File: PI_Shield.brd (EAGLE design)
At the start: 160 x 100 mm, 29 parts, among them Q2 220mA/50V/3.5Ω, Y1 ECS-80-S-4X

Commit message: Minor Changes with Schematic
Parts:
- moved PCB1 157.5 mm to (57.1, 1.27), turned to 90 degrees
- moved U$1 73.8 mm to (14.3, 18.0)
- moved U$3 51.7 mm to (23.4, 53.2)
- moved Y1 34.1 mm to (-66.3, 33.3)
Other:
- board size 160 x 100 mm -> 60 x 66.5 mm

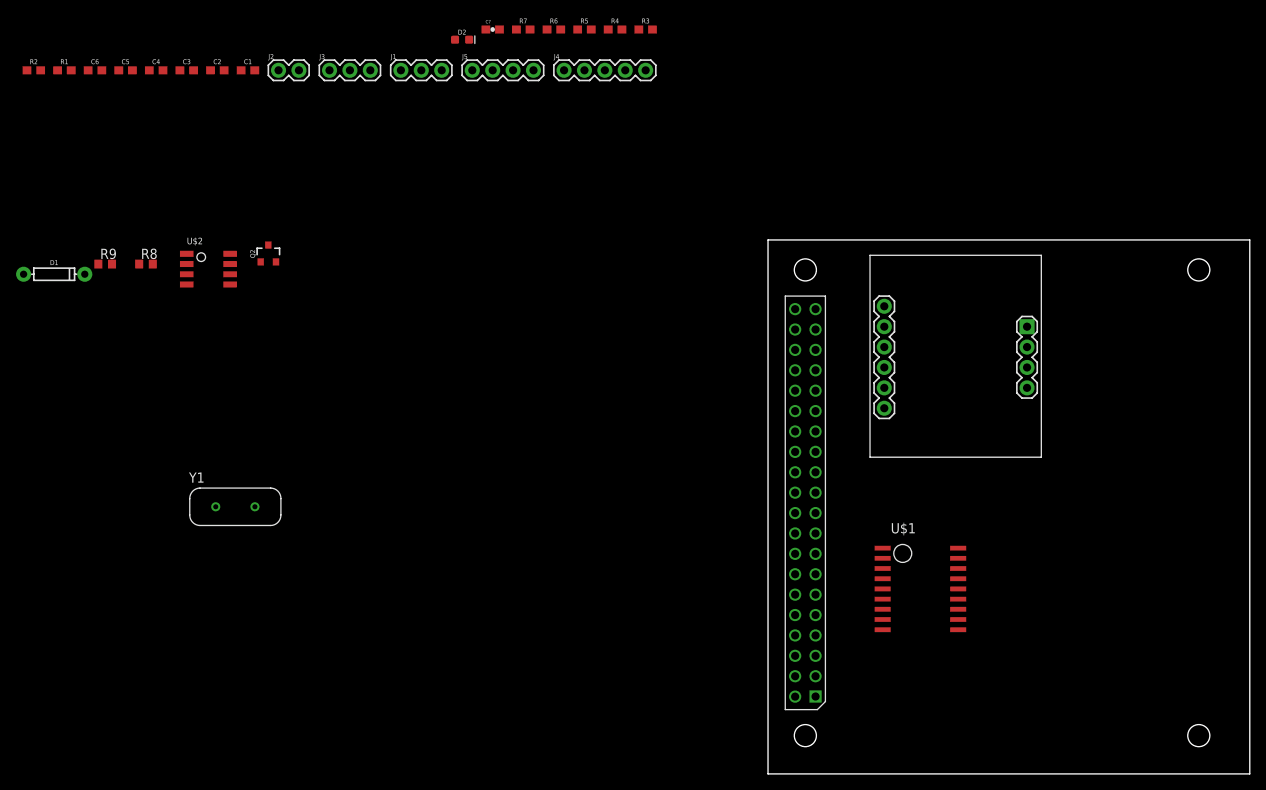
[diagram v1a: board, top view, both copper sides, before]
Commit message: Starting to Route Board
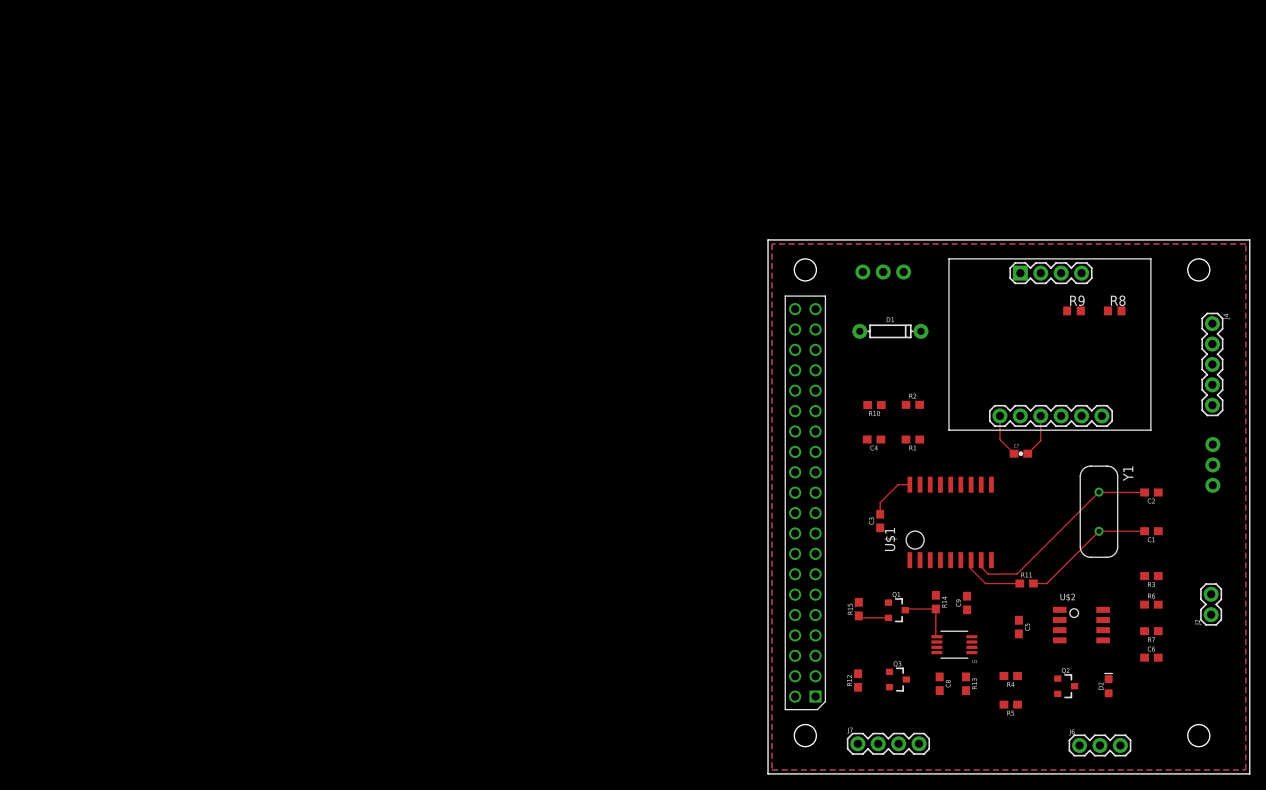
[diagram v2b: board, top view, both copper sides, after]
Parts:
- removed J5: (no value), SparkFun-Connectors:1X04
- added C8, C9: .1uF, SparkFun-Capacitors:0603
- added J6: (no value), SparkFun-Connectors:1X03
- added J7: (no value), SparkFun-Connectors:1X04
- added Q1, Q3: 220mA/50V/3.5Ω, SparkFun-DiscreteSemi:SOT23-3
- added R10: 47, SparkFun-Resistors:0603
- added R11: 0, SparkFun-Resistors:0603
- added R12, R13, R14, R15: 10k, SparkFun-Resistors:0603
- added U1: MAX1136EUA-T, MAX1136EUA-T:21-0036K
- C1, C2: value 22pF -> 18pF
- R3: value (none) -> 0
- moved C6 150.5 mm to (47.8, 14.5)
- moved J2 134.5 mm to (55.2, 19.8), turned to 90 degrees
- moved C5 131.1 mm to (31.2, 18.3), turned to 270 degrees
- moved C2 127.7 mm to (47.8, 35.1), turned to 180 degrees
- moved C1 126.3 mm to (47.8, 30.2), turned to 180 degrees
- moved J3 121.5 mm to (55.4, 35.9), flipped to the bottom, turned to 90 degrees
- moved R8 120.8 mm to (43.2, 57.7)
- moved R9 120.8 mm to (38.1, 57.7)
- moved U$2 117.4 mm to (36.3, 16.6)
- moved R2 117.1 mm to (18.0, 46.0)
- moved R1 115.2 mm to (18.0, 41.7), turned to 180 degrees
- moved D2 113.9 mm to (42.4, 10.9), turned to 90 degrees
- moved Q2 113.0 mm to (37.1, 10.9), turned to 270 degrees
- moved R7 108.3 mm to (47.8, 17.8), turned to 180 degrees
- moved Y1 107.6 mm to (41.2, 32.7), turned to 270 degrees
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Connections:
- new net AIN: J6.1, U1.1
- new net N$6: D1.A, R10.2
- new net N$7: C8.2
- new net SCL_ADC: Q1.3, R14.2, U1.5
- new net SDA_ADC: Q3.3, R13.2, U1.6
- net 3V3: now also Q1.1, Q3.1, R12.2, R15.2
- net 5V: now also C8.1, C9.1, J6.2, J7.4, R13.1, R14.1, U1.4, U1.8; no longer J5.4
- net GND: now also C9.2, J6.3, J7.1, U1.7; no longer J5.1
- net IMU_RESET: now also PCB1.P$33; no longer PCB1.P$7
- net INT: now also PCB1.P$35, U$3.INT; no longer PCB1.P$26
- net N$3: now also R10.1; no longer D1.A
- net OSC2: now also R11.1, R11.2
- net RESET: now also PCB1.P$15; no longer PCB1.P$22
- net SCL: now also J7.2, Q1.2, R15.1; no longer J5.2
- net SDA: now also J7.3, Q3.2, R12.1; no longer J5.3
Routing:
- net OSC1: track 0.00 -> 25.8 mm
- net OSC2: track 0.00 -> 24.5 mm
- net 3V3: track 0.00 -> 11.5 mm
- net SCL_ADC: track 0.00 -> 7.36 mm
- net GND: track 0.00 -> 5.38 mm
- net SCL: track 0.00 -> 3.79 mm
- added copper zone on layer 1, net GND
- added copper zone on layer 16, net GND

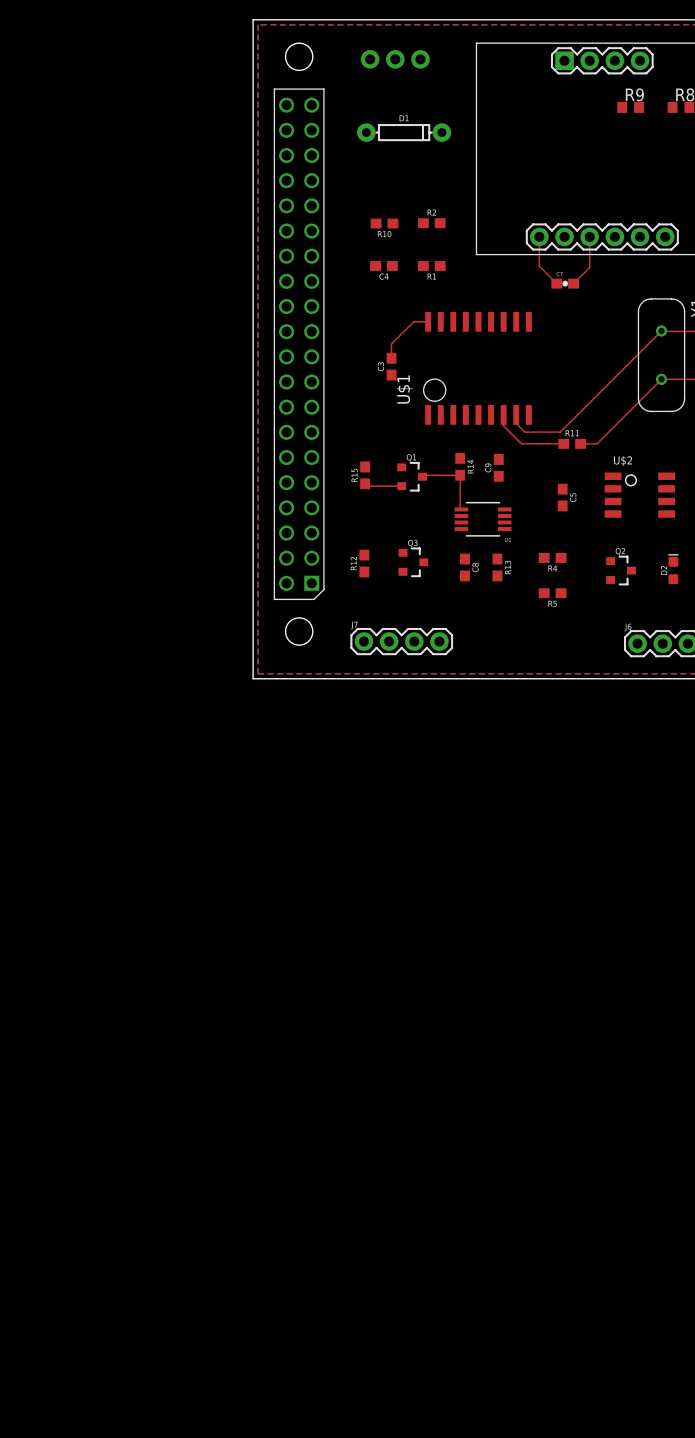
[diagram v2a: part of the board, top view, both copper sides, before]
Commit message: Added Current Sensor
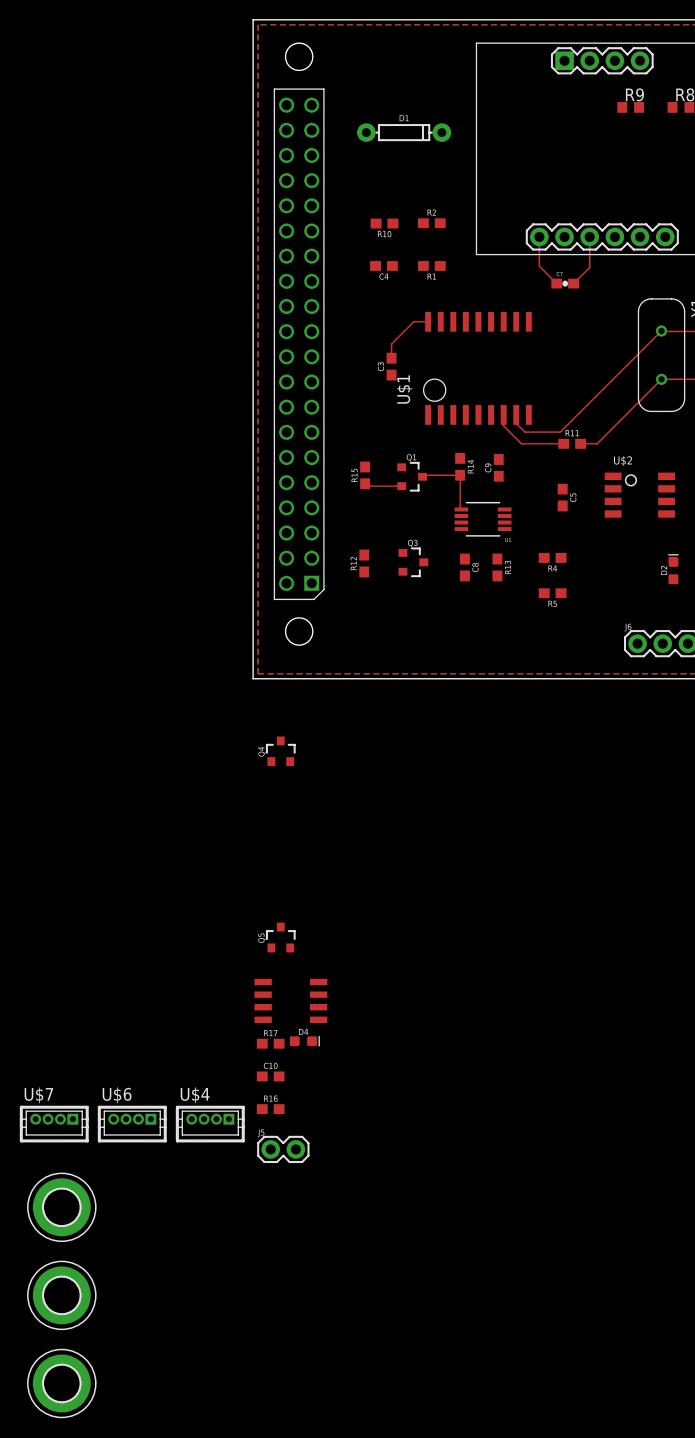
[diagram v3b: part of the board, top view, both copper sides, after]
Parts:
- removed J1: (no value), SparkFun-Connectors:1X03
- removed J7: (no value), SparkFun-Connectors:1X04
- removed Q2: 220mA/50V/3.5Ω, SparkFun-DiscreteSemi:SOT23-3
- added C10: .1uF, SparkFun-Capacitors:0603
- added D4: (no value), SparkFun-LED:LED-0603
- added H1, H2, H3: MOUNT-PAD-ROUND3.6, holes:3,6-PAD
- added J5: (no value), SparkFun-Connectors:1X02
- added Q4: 220mA/50V/3.5Ω, SparkFun-DiscreteSemi:SOT23-3
- added Q5: 2.5A/30V/105mΩ, SparkFun-DiscreteSemi:SOT23-3
- added R16: 1k, SparkFun-Resistors:0603
- added R17: 150, SparkFun-Resistors:0603
- added U$4, U$6, U$7: DF13-4P-1.25DSA, con-hirose-df13:DF13-4P-1.25DSA
- added U$5: ACS711, ACS711_ameter:ACS711
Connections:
- new net AMP_FAULT: Q5.1, R16.1, U$5.FAULT
- new net AMP_OUT: U$5.VIOUT, U1.2
- new net N$10: Q5.2, R17.2
- new net N$11: D4.A, R17.1
- new net N$8: C10.1, U$5.VCC
- new net PI_POWER: J5.2, U$5.IP1-, U$5.IP2-
- net 3V3: now also H2.B3,6, U$4.P$1, U$6.P$1, U$7.P$1; no longer J1.2
- net 5V: now also H1.B3,6, Q5.3, R16.2, U$5.IP1+, U$5.IP2+; no longer J1.3, J7.4
- net FAULT: now also Q4.1; no longer Q2.1
- net GND: now also C10.2, D4.C, H3.B3,6, J5.1, Q4.2, U$4.P$4, U$5.GND, U$6.P$4, U$7.P$4; no longer J1.1, J7.1, Q2.2
- net N$4: now also Q4.3; no longer Q2.3
- net SCL: now also U$4.P$3, U$6.P$3, U$7.P$3; no longer J7.2
- net SDA: now also U$4.P$2, U$6.P$2, U$7.P$2; no longer J7.3

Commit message: Almost Done with Board
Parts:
- removed C7: 0.1u, SparkFun-Passives:0603-CAP
- removed H2: MOUNT-PAD-ROUND3.6, holes:3,6-PAD
- removed J2: (no value), SparkFun-Connectors:1X02
- removed J6: (no value), SparkFun-Connectors:1X03
- added C11, C12: .1uF, SparkFun-Capacitors:0603
- added C13: .1u, SparkFun-Capacitors:0603
- added D3: (no value), SparkFun-LED:LED-0603
- added R18: 150, SparkFun-Resistors:0603
- added R19: 0, SparkFun-Resistors:0603
- added U$10: T2I, BackplaneParts:T2I
- added U$11, U$9: DF13-3P-1.25DSA, con-hirose-df13:DF13-3P-1.25DSA
- added U$8: T2I5P, BackplaneParts:T2I5P
- added U2: AZ1117EH-3.3TRG1, AZ1117EH-3.3TRG1:SOT230P700X180-4N
- D1: value 200mA/100V/1V -> 250mA/100V; device SparkFun-DiscreteSemi:DIODE-1N4148 -> SparkFun-DiscreteSemi:SOD-323
- R8, R9: device resistor:R0603 -> SparkFun-Resistors:0603
- moved H1 162.3 mm to (75.2, 78.7)
- moved H3 121.2 mm to (74.7, 5.38)
- moved J5 119.0 mm to (75.3, 46.1), turned to 90 degrees
- moved C10 89.0 mm to (30.8, 44.0), turned to 90 degrees
- moved U$4 86.8 mm to (4.80, 41.9), turned to 90 degrees
- moved R16 85.2 mm to (39.2, 33.1), turned to 90 degrees
- moved D4 84.8 mm to (53.5, 33.0), turned to 270 degrees
- moved R17 84.6 mm to (49.5, 32.9), turned to 270 degrees
- moved U$6 75.4 mm to (4.80, 29.0), turned to 90 degrees
- moved Q5 72.1 mm to (44.0, 32.9)
- moved U$5 70.2 mm to (27.3, 33.6)
- moved Q4 68.4 mm to (64.0, 23.4), turned to 180 degrees
- moved U$7 66.4 mm to (4.80, 17.1), turned to 90 degrees
- moved R9 55.7 mm to (52.3, 3.78), turned to 90 degrees
- moved R8 54.1 mm to (48.1, 3.73), turned to 90 degrees
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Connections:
- removed net N$7: C8.2
- removed net N$8: C10.1, U$5.VCC
- new net DI: PCB1.P$16, U$9.P$2
- new net IMU_INT: U$3.INT
- new net IMU_NET: PCB1.P$31
- new net N$9: D3.A, R18.1
- net 3V3: now also C10.1, C12.1, C13.1, R8.1, R9.1, U$5.VCC, U2.2, U2.4; no longer C7.1, H2.B3,6, R8.2, R9.2
- net 5V: now also C11.1, R18.2, U$11.P$2, U$8.P$5, U$8.P$6, U$9.P$1, U2.3; no longer J6.2
- net AIN: now also U$11.P$1; no longer J6.1
- net CANH: now also J5.2, U$10.2; no longer J2.2
- net CANL: now also J5.1, U$10.3; no longer J2.1
- net GND: now also C11.2, C12.2, C13.2, C8.2, D3.C, PCB1.P$9, U$11.P$3, U$8.P$2, U$8.P$3, U$9.P$3, U2.1; no longer C7.2, J5.1, J6.3
- net INT: no longer U$3.INT
- net OSC1: now also R19.1, R19.2
- net PI_POWER: now also PCB1.P$2, PCB1.P$4; no longer J5.2
- net RESET: no longer PCB1.P$15
- net SCL: now also R9.2; no longer R9.1
- net SDA: now also R8.2; no longer R8.1
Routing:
- net 3V3: track 11.5 -> 375.4 mm
- net 5V: track 0.00 -> 287.9 mm
- net SDA: track 0.00 -> 116.0 mm, vias 0 -> 4
- net SCL: track 3.79 -> 81.1 mm, vias 0 -> 2
- net PI_POWER: track 0.00 -> 72.8 mm
- net CS: track 0.00 -> 66.0 mm, vias 0 -> 2
- net MISO: track 0.00 -> 65.2 mm, vias 0 -> 2
- net MOSI: track 0.00 -> 63.9 mm, vias 0 -> 3
- net CANL: track 0.00 -> 58.2 mm, vias 0 -> 3
- net CANH: track 0.00 -> 58.0 mm, vias 0 -> 2
- net CLK: track 0.00 -> 57.0 mm, vias 0 -> 1
- net AMP_OUT: track 0.00 -> 35.7 mm, vias 0 -> 2
- net AIN: track 0.00 -> 33.8 mm, vias 0 -> 1
- net INT: track 0.00 -> 28.2 mm, vias 0 -> 1
- net TXCAN: track 0.00 -> 26.7 mm, vias 0 -> 3
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- added copper zone on layer 16, net SCL
- added copper zone on layer 16, net SDA
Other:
- board size 60 x 66.5 mm -> 80 x 85 mm

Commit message: Almost Done
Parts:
- moved U$11 35.9 mm to (4.91, 42.2)
- moved C10 9.71 mm to (33.5, 34.7), turned to 270 degrees
- moved U$4 9.65 mm to (4.92, 32.2)
- moved U$7 9.65 mm to (4.92, 7.45)
- moved U$6 9.65 mm to (4.92, 19.3)
- moved C12 2.38 mm to (33.5, 62.6), turned to 0 degrees
- moved R16 1.81 mm to (40.3, 34.5)
- moved R17 1.81 mm to (50.7, 34.3)
- moved D4 1.81 mm to (54.7, 34.4)
- moved Q5 1.81 mm to (45.2, 34.3)
- moved R15 1.14 mm to (19.9, 22.5)
- moved R12 0.13 mm to (24.8, 10.2), turned to 90 degrees
- turned Q3 to 270 degrees
- turned R11 to 180 degrees
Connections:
- removed net IMU_NET: PCB1.P$31
- new net OSC1_XTAL: C2.2, R19.1, Y1.1
- new net OSC2_XTAL: C1.2, R11.1, Y1.2
- net CLK: now also J4.2; no longer J4.3
- net CS: now also J4.5; no longer J4.2
- net DI: now also PCB1.P$36; no longer PCB1.P$16
- net IMU_INT: now also PCB1.P$15
- net IMU_RESET: now also PCB1.P$13; no longer PCB1.P$33
- net MOSI: now also J4.3; no longer J4.5
- net OSC1: no longer C2.2, R19.1, Y1.1
- net OSC2: no longer C1.2, R11.1, Y1.2
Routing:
- net 3V3: track 375.4 -> 460.8 mm
- net IMU_RESET: track 0.00 -> 52.2 mm, vias 0 -> 2
- net IMU_INT: track 0.00 -> 49.8 mm, vias 0 -> 2
- net SCL: track 81.1 -> 121.0 mm
- net 5V: track 287.9 -> 258.3 mm
- net SDA: track 116.0 -> 94.1 mm, vias 4 -> 2
- net MISO: track 65.2 -> 51.8 mm, vias 2 -> 1
- net AMP_FAULT: track 9.55 -> 22.4 mm
- net OSC2: track 16.3 -> 4.84 mm
- net OSC1: track 16.1 -> 4.79 mm
- net OSC1_XTAL: track 0.00 -> 11.3 mm
- net OSC2_XTAL: track 0.00 -> 11.2 mm
- net DI: track 0.00 -> 9.99 mm
- net MOSI: track 63.9 -> 54.2 mm
- net AIN: track 33.8 -> 41.3 mm
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- added copper zone on layer 1, net 3V3
- added copper zone on layer 1, net 5V
- added copper zone on layer 1, net SDA
- removed copper zone on layer 16, net SDA
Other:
- board size 80 x 85 mm -> 80.1 x 86.7 mm

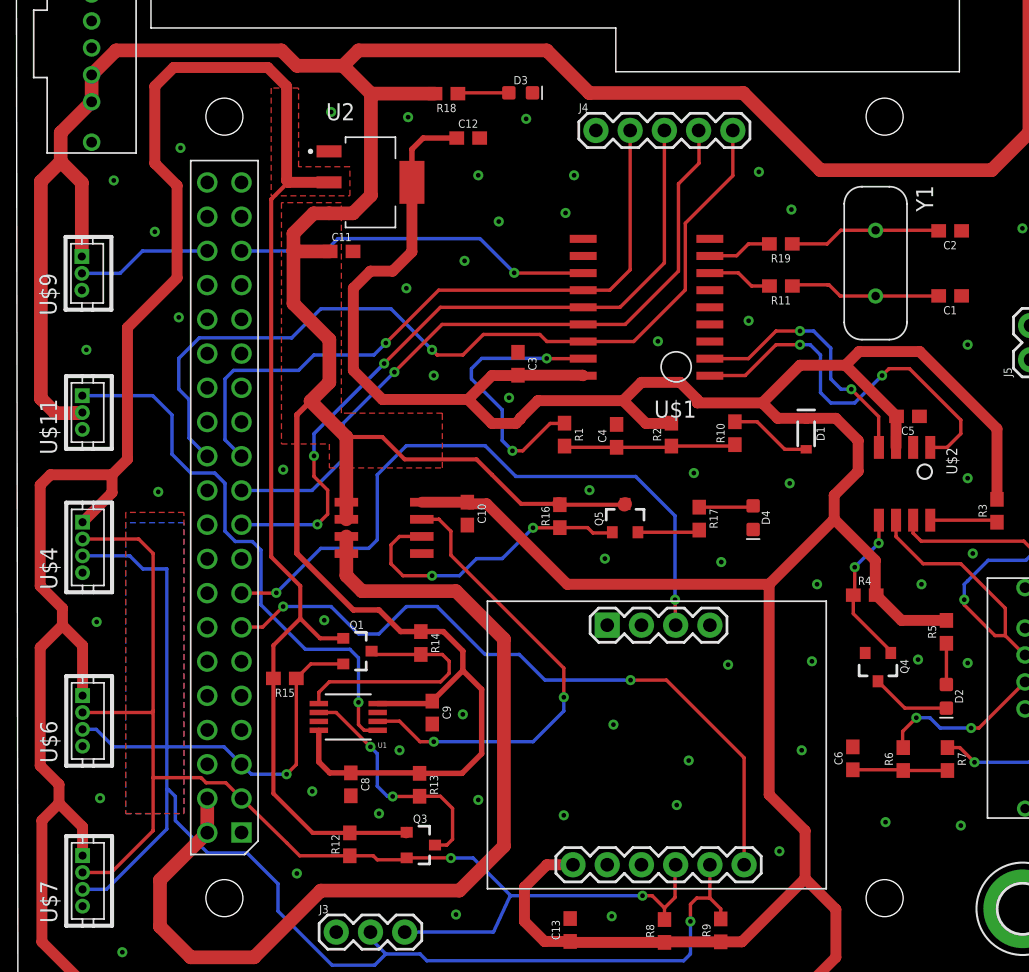
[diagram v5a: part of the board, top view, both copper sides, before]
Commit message: Minor Changes to Board
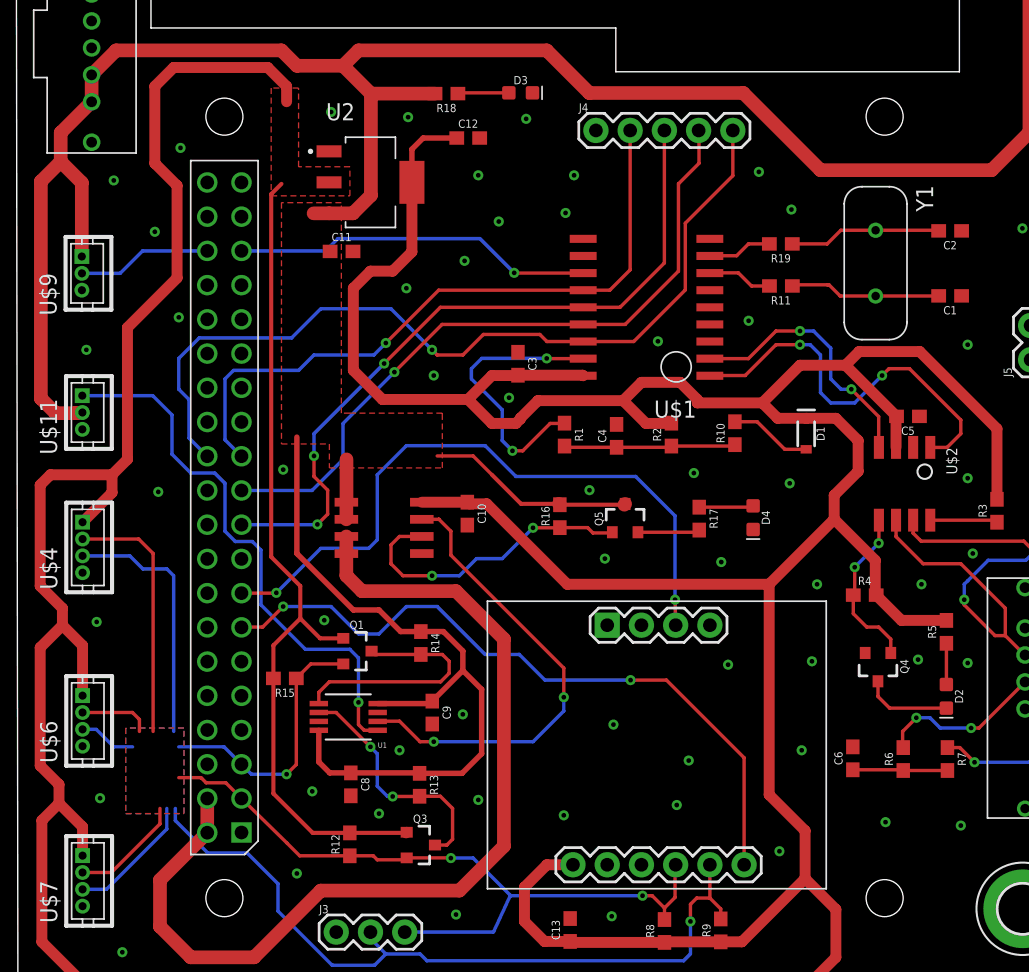
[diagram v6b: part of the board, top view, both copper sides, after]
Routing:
- net 5V: track 258.3 -> 223.5 mm
- net SCL: track 121.0 -> 110.3 mm
- net 3V3: track 460.8 -> 451.4 mm
- net SDA: track 94.1 -> 86.7 mm
- net N$4: track 5.90 -> 6.56 mm
- net FAULT: track 11.8 -> 12.3 mm
